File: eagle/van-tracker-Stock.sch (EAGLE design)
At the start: 13 parts, among them K1 CP1-12V, Q1 TIP122

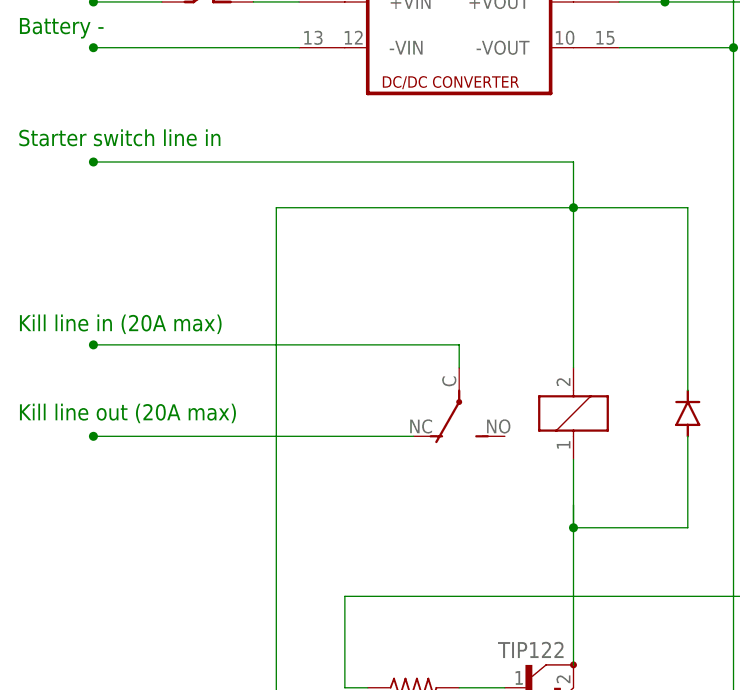
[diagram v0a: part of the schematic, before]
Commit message: 1.Use power from starter to power relay coil
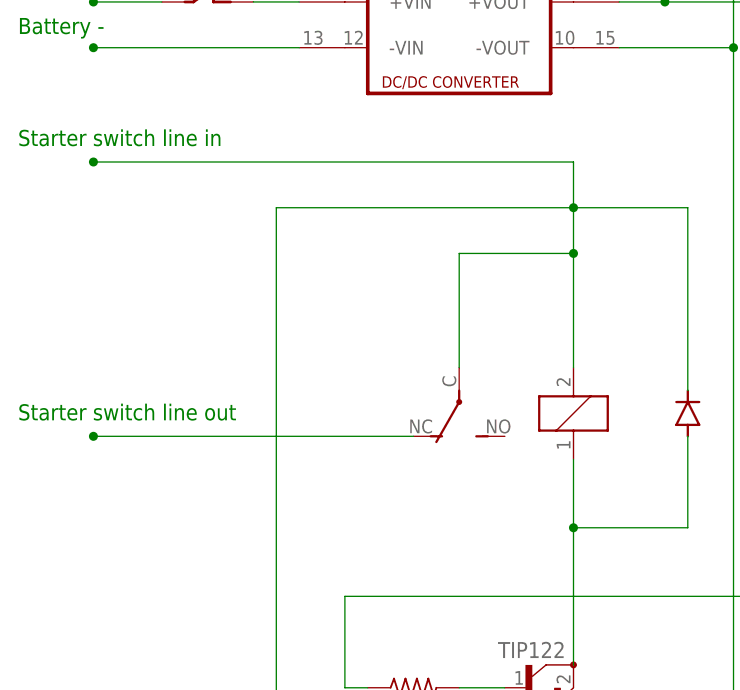
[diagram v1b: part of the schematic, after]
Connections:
- removed net N$17: 10K_OHMS.1, D1.C, K11.2
- net N$7: now also 10K_OHMS.1, D1.C, K11.2
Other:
- note added: "Starter switch line out"
- note removed: "Kill line in (20A max)"
- note removed: "Kill line out (20A max)"
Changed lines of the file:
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@@
 <sheet>
 <plain>
-<text x="-41.402" y="29.464" size="1.778" layer="91">Kill line in (20A max)</text>
-<text x="-41.402" y="19.558" size="1.778" layer="91">Kill line out (20A max)</text>
 <text x="-41.402" y="50.038" size="1.778" layer="91">Starter switch line in</text>
 <text x="-41.402" y="67.564" size="1.778" layer="91">Battery +</text>
 <text x="-41.402" y="62.484" size="1.778" layer="91">Battery -</text>
+<text x="-41.402" y="19.558" size="1.778" layer="91">Starter switch line out</text>
 </plain>
 <instances>
@@
 <wire x1="99.06" y1="91.44" x2="99.06" y2="86.28" width="0.1524" layer="91"/>
 <wire x1="99.06" y1="86.28" x2="93.76" y2="86.28" width="0.1524" layer="91"/>
-</segment>
-</net>
-<net name="N$7" class="0">
-<segment>
-<pinref part="K1" gate="2" pin="P"/>
-<wire x1="7.62" y1="25.4" x2="7.62" y2="27.94" width="0.1524" layer="91"/>
-<wire x1="7.62" y1="27.94" x2="-33.02" y2="27.94" width="0.1524" layer="91"/>
-<junction x="-33.02" y="27.94"/>
 </segment>
 </net>
@@
 </segment>
 </net>
-<net name="N$17" class="0">
-<segment>
-<pinref part="K1" gate="1" pin="2"/>
-<wire x1="20.32" y1="43.18" x2="20.32" y2="25.4" width="0.1524" layer="91"/>
-<pinref part="D1" gate="1" pin="C"/>
-<wire x1="33.02" y1="22.86" x2="33.02" y2="43.18" width="0.1524" layer="91"/>
-<wire x1="33.02" y1="43.18" x2="20.32" y2="43.18" width="0.1524" layer="91"/>
-<wire x1="20.32" y1="43.18" x2="20.32" y2="48.26" width="0.1524" layer="91"/>
-<junction x="20.32" y="43.18"/>
-<junction x="-33.02" y="48.26"/>
-<wire x1="20.32" y1="48.26" x2="-33.02" y2="48.26" width="0.1524" layer="91"/>
-<pinref part="10K_OHMS" gate="G$1" pin="1"/>
-<wire x1="-12.7" y1="-30.48" x2="-2.54" y2="-30.48" width="0.1524" layer="91"/>
-<wire x1="20.32" y1="43.18" x2="-12.7" y2="43.18" width="0.1524" layer="91"/>
-<wire x1="-12.7" y1="43.18" x2="-12.7" y2="-30.48" width="0.1524" layer="91"/>
-</segment>
-</net>
 <net name="N$5" class="0">
 <segment>
@@
 <wire x1="33.02" y1="17.78" x2="33.02" y2="7.62" width="0.1524" layer="91"/>
 <wire x1="33.02" y1="7.62" x2="20.32" y2="7.62" width="0.1524" layer="91"/>
+<pinref part="Q1" gate="G$1" pin="C"/>
+<wire x1="20.32" y1="7.62" x2="20.32" y2="-7.62" width="0.1524" layer="91"/>
 <junction x="20.32" y="7.62"/>
-<pinref part="Q1" gate="G$1" pin="C"/>
-<wire x1="20.32" y1="7.62" x2="20.32" y2="10.16" width="0.1524" layer="91"/>
-<wire x1="20.32" y1="7.62" x2="20.32" y2="-7.62" width="0.1524" layer="91"/>
 </segment>
 </net>
@@
 </segment>
 </net>
+<net name="N$7" class="0">
+<segment>
+<pinref part="K1" gate="2" pin="P"/>
+<wire x1="7.62" y1="25.4" x2="7.62" y2="38.1" width="0.1524" layer="91"/>
+<wire x1="-33.02" y1="48.26" x2="20.32" y2="48.26" width="0.1524" layer="91"/>
+<pinref part="K1" gate="1" pin="2"/>
+<wire x1="20.32" y1="43.18" x2="20.32" y2="38.1" width="0.1524" layer="91"/>
+<pinref part="D1" gate="1" pin="C"/>
+<wire x1="20.32" y1="38.1" x2="20.32" y2="25.4" width="0.1524" layer="91"/>
+<wire x1="33.02" y1="22.86" x2="33.02" y2="43.18" width="0.1524" layer="91"/>
+<wire x1="33.02" y1="43.18" x2="20.32" y2="43.18" width="0.1524" layer="91"/>
+<wire x1="20.32" y1="48.26" x2="20.32" y2="43.18" width="0.1524" layer="91"/>
+<junction x="20.32" y="43.18"/>
+<junction x="-33.02" y="48.26"/>
+<pinref part="10K_OHMS" gate="G$1" pin="1"/>
+<wire x1="-12.7" y1="-30.48" x2="-2.54" y2="-30.48" width="0.1524" layer="91"/>
+<wire x1="-12.7" y1="43.18" x2="-12.7" y2="-30.48" width="0.1524" layer="91"/>
+<wire x1="20.32" y1="43.18" x2="-12.7" y2="43.18" width="0.1524" layer="91"/>
+<wire x1="7.62" y1="38.1" x2="20.32" y2="38.1" width="0.1524" layer="91"/>
+<junction x="20.32" y="38.1"/>
+</segment>
+</net>
